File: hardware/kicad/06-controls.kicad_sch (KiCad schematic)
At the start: 38 parts, among them SW1 UP, SW10 SELECT, SW11 L, SW12 R, SW13 MENU, SW2 DOWN, SW3 LEFT, SW4 RIGHT, SW5 A, SW6 B, SW7 X, SW8 Y, SW9 START

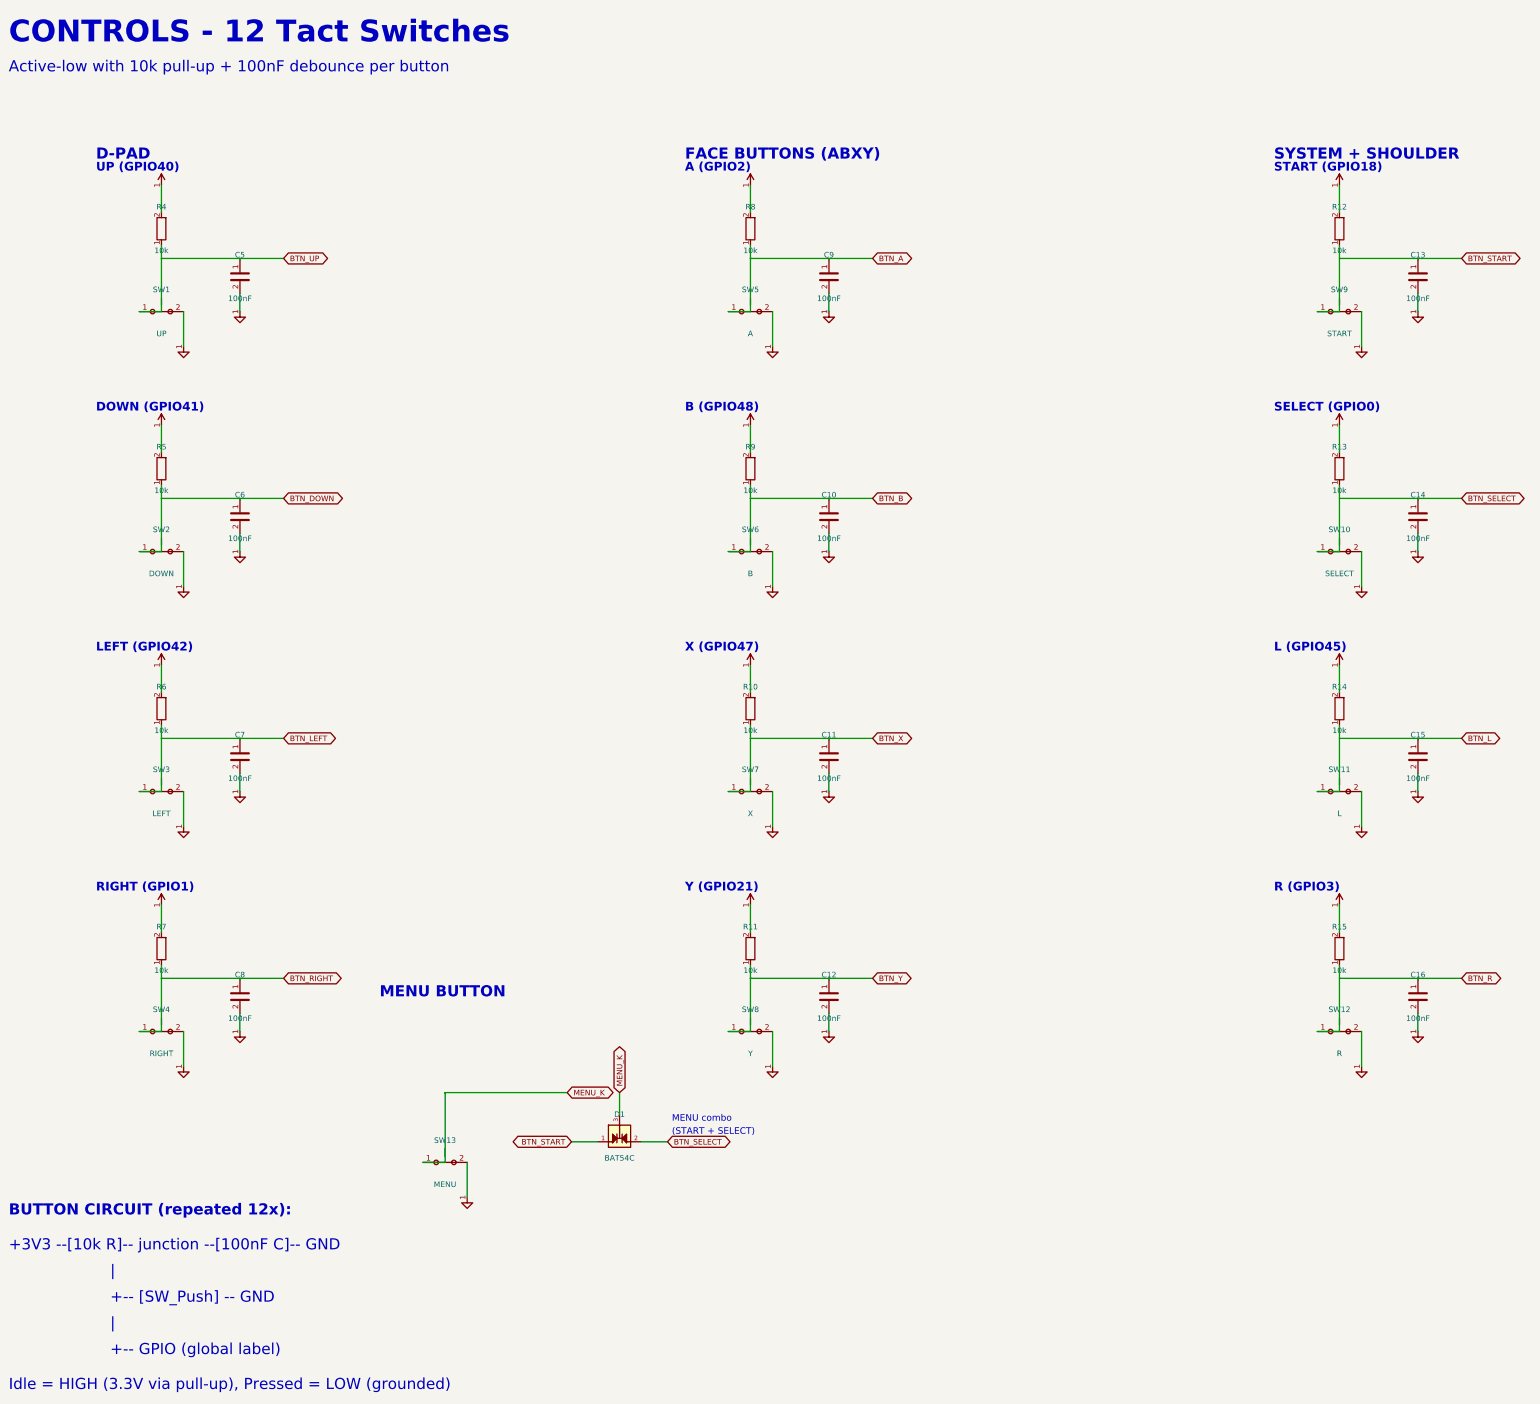
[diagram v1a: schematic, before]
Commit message: feat(containment): layer 6 — ERC warning burn-down, 676 to ZERO, gate at all severities
Three root causes, three fixes in the schematic generator:

- 507 endpoint_off_grid: sheets lay out on a human 1 mm grid while KiCad
  connects on 1.27 mm. snap() in kicad_primitives now grid-snaps every
  connection-bearing coordinate at emission. Snapping is monotonic and
  distributes over the library's grid-multiple pin offsets, so points
  that coincided before still coincide after; zero-length stub wires
  that collapse onto their anchor are dropped.
- The stragglers came from three symbols whose pin connection points
  were themselves off-grid: BAT54C (±5.0 → ±5.08, top 5.0 → 5.08, used
  by D1 and Q1), USBLC6-2SC6 (±10.0 → ±10.16), Speaker (±0.635 →
  ±1.27). Their sheet wiring moved with them in the same commit.
- 169 lib_symbol_issues: bare lib_ids referenced library "" which no
  configuration includes. Symbols are now emu:<name>, resolved by a
  generated hardware/kicad/sym-lib-table + emu.kicad_sym built from the
  same SYMBOLS strings as the embedded caches — cache and library
  cannot disagree by construction.

verify_erc now runs --severity-all against a ZERO baseline: from zero,
any new warning is a regression a specific change introduced. The
website's per-sheet SVGs/PDFs are re-rendered, and the "Download all
sheets" PDF — a one-off hand merge nothing regenerated, stale since the
R25 respin — is now merged by render-schematics.sh from the exported
sheets.

Suite: 85/85 green; netlist_diff vs PCB confirms connectivity unchanged.

Co-Authored-By: Claude Fable 5 <noreply@anthropic.com>
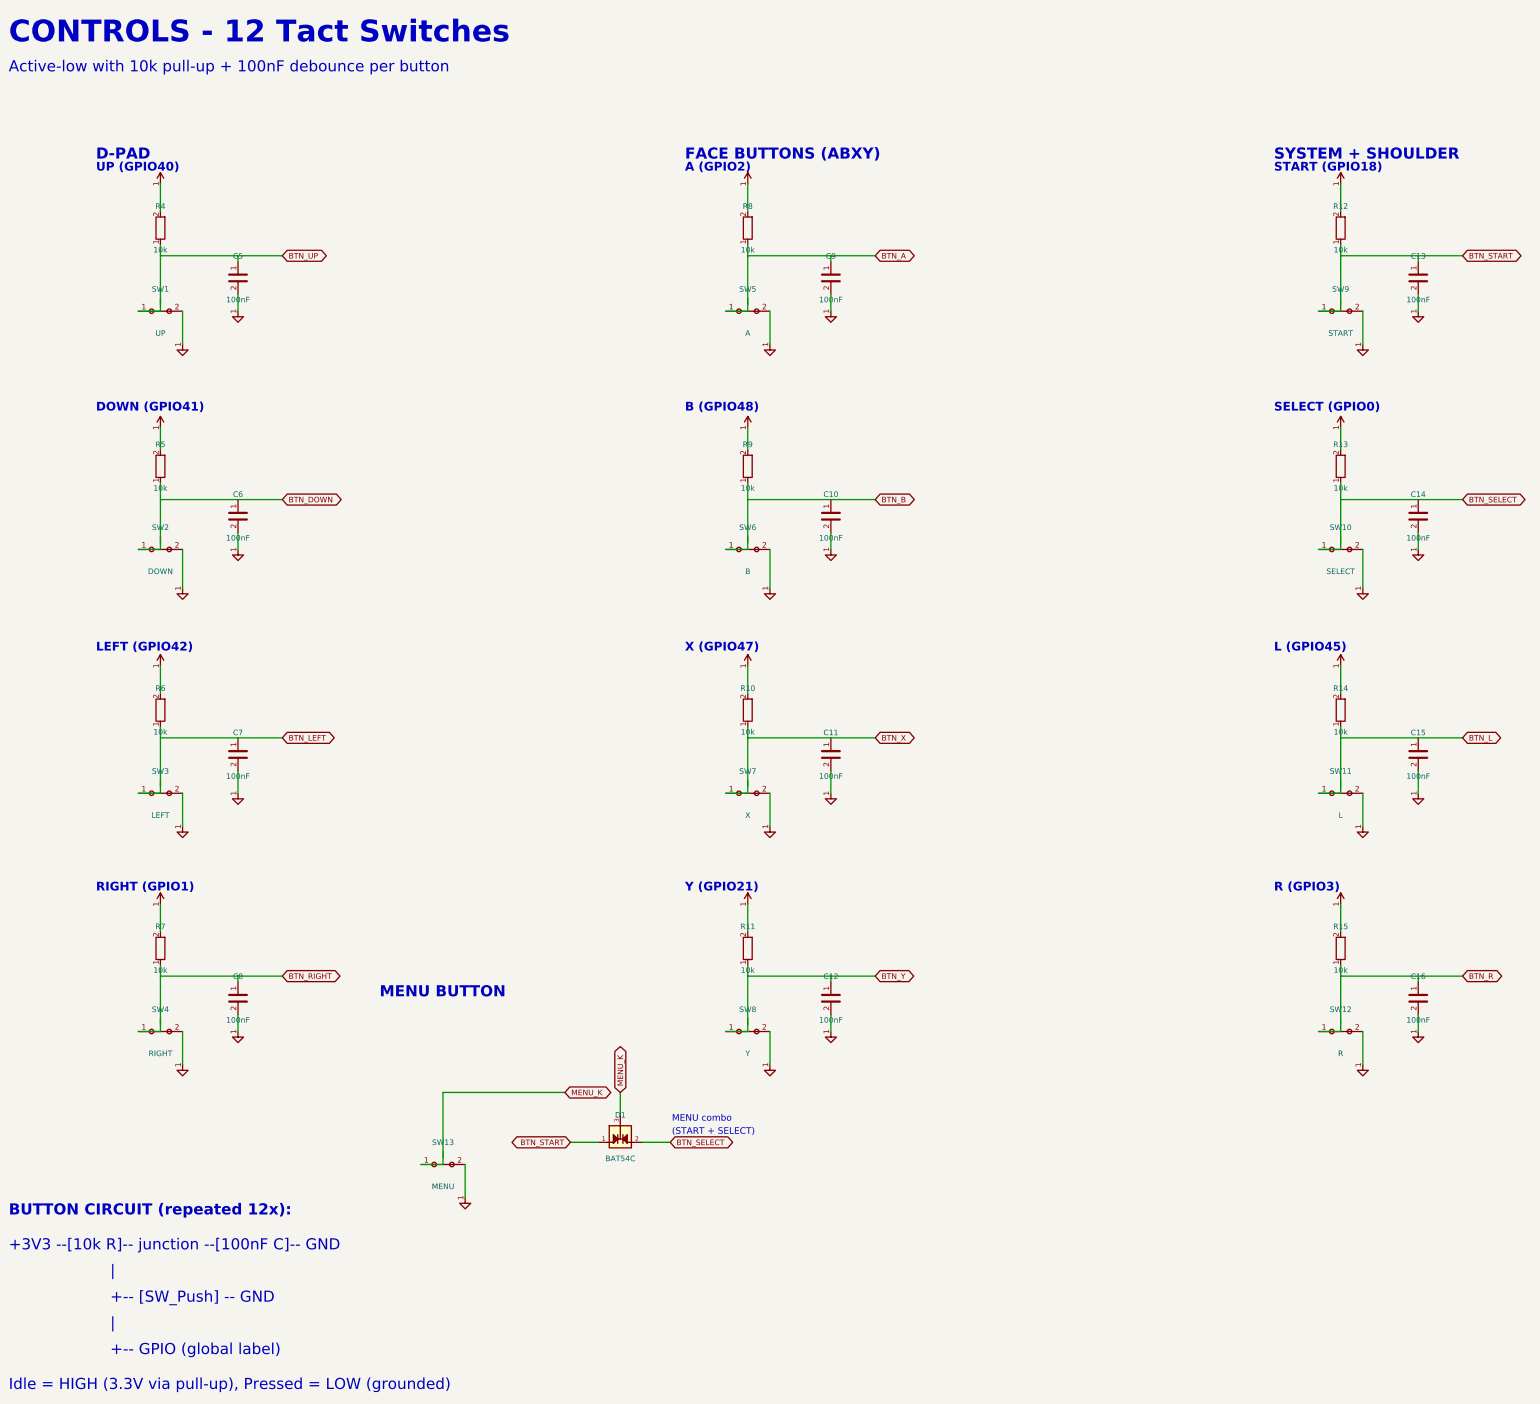
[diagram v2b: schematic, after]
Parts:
- removed C10, C11, C12, C13, C14, C15, C16, C7, C8, C9: 100nF, symbol C
- removed D1: BAT54C, symbol BAT54C
- removed R10, R11, R12, R13, R14, R6, R7, R8, R9: 10k, symbol R
- removed SW10: SELECT, symbol SW_Push
- removed SW11: L, symbol SW_Push
- removed SW12: R, symbol SW_Push
- removed SW13: MENU, symbol SW_Push
- removed SW2: DOWN, symbol SW_Push
- removed SW3: LEFT, symbol SW_Push
- removed SW4: RIGHT, symbol SW_Push
- removed SW5: A, symbol SW_Push
- removed SW6: B, symbol SW_Push
- removed SW7: X, symbol SW_Push
- removed SW8: Y, symbol SW_Push
- removed SW9: START, symbol SW_Push
- added C10, C11, C12, C13, C14, C15, C7, C8, C9: 100nF, symbol emu:C
- added D1: BAT54C, symbol emu:BAT54C
- added R10, R11, R12, R13, R14, R15, R6, R7, R8, R9: 10k, symbol emu:R
- added SW10: SELECT, symbol emu:SW_Push
- added SW11: L, symbol emu:SW_Push
- added SW12: R, symbol emu:SW_Push
- added SW13: MENU, symbol emu:SW_Push
- added SW2: DOWN, symbol emu:SW_Push
- added SW3: LEFT, symbol emu:SW_Push
- added SW4: RIGHT, symbol emu:SW_Push
- added SW5: A, symbol emu:SW_Push
- added SW6: B, symbol emu:SW_Push
- added SW7: X, symbol emu:SW_Push
- added SW8: Y, symbol emu:SW_Push
- added SW9: START, symbol emu:SW_Push
- C16: renamed from R15; value 10k -> 100nF; symbol R -> emu:C
- C5, C6: symbol C -> emu:C
- R4, R5: symbol R -> emu:R
- SW1: symbol SW_Push -> emu:SW_Push
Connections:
- net +3V3: now also R10.2, R11.2, R12.2, R13.2, R14.2, R15.2, R6.2, R7.2, R8.2, R9.2; no longer C16.2
- net BTN_A: now also C9.1, R8.1, SW5.1
- net BTN_B: now also C10.1, R9.1, SW6.1
- net BTN_DOWN: now also SW2.1
- net BTN_L: now also C15.1, R14.1, SW11.1
- net BTN_LEFT: now also C7.1, R6.1, SW3.1
- net BTN_R: now also R15.1, SW12.1
- net BTN_RIGHT: now also C8.1, R7.1, SW4.1
- net BTN_SELECT: now also C14.1, D1.2, R13.1, SW10.1
- net BTN_START: now also C13.1, D1.1, R12.1, SW9.1
- net BTN_X: now also C11.1, R10.1, SW7.1
- net BTN_Y: now also C12.1, R11.1, SW8.1
- net GND: now also C16.2, C10.2, C11.2, C12.2, C13.2, C14.2, C15.2, C7.2, C8.2, C9.2, SW10.2, SW11.2, SW12.2, SW13.2, SW2.2, SW3.2, SW4.2, SW5.2, SW6.2, SW7.2, SW8.2, SW9.2
- net MENU_K: now also D1.3, SW13.1
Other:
- moved on the sheet: C5, R5

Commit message: schematic: zero rendered text overlaps + real P-MOSFET artwork for Q1/Q2
The rendered sheets carried 75 text-on-text collisions the overlap gate
could not see: its model missed pin-number digits, KiCad's mirrored
field justification on 180-degree symbols, and global-label extents.
Root fixes in the generator:

- symbol() now places Reference/Value per part class: beside the body
  for two-pin verticals (R/C/L/Battery), stacked above for LEDs and the
  big ICs whose bottom pin numbers the old centred Value printed over,
  with per-call overrides where a zone is tight. On 180-rotated symbols
  the emitted justification is pre-mirrored, because KiCad flips it.
- Q1/Q2 get PMOS_SOT23 — same pin coordinates as the BAT54C symbol they
  were drawn with (wires and netlist untouched), but the artwork is now
  a P-MOSFET instead of a dual Schottky diode.
- Sheet-level relayouts: decoupling row on 02 spread to 11 mm pitch,
  menu-combo D1 zone on 06, FPC header on 03, PAM bias notes on 04,
  IP5306 KEY exit and the whole power-switch zone on 01.
- ESP32 module pin 41 name blanked — two "GND"s 2.54 mm apart printed
  into each other; number, type and net unchanged.

New gate: verify_schematic_render_overlaps.py exports each sheet to SVG
via kicad-cli and fails if any two DRAWN text runs intersect — ground
truth instead of a re-derived model (47 hits on the old sheet 01, 0
now). Wired into verify-all; dispatch mutation tests 14/14.

Netlist invariance: verify_netlist_diff 4/4, ERC clean at every
severity, schematic-PCB sync green. Website SVG/PDF re-rendered.

Co-Authored-By: Claude Fable 5 <noreply@anthropic.com>
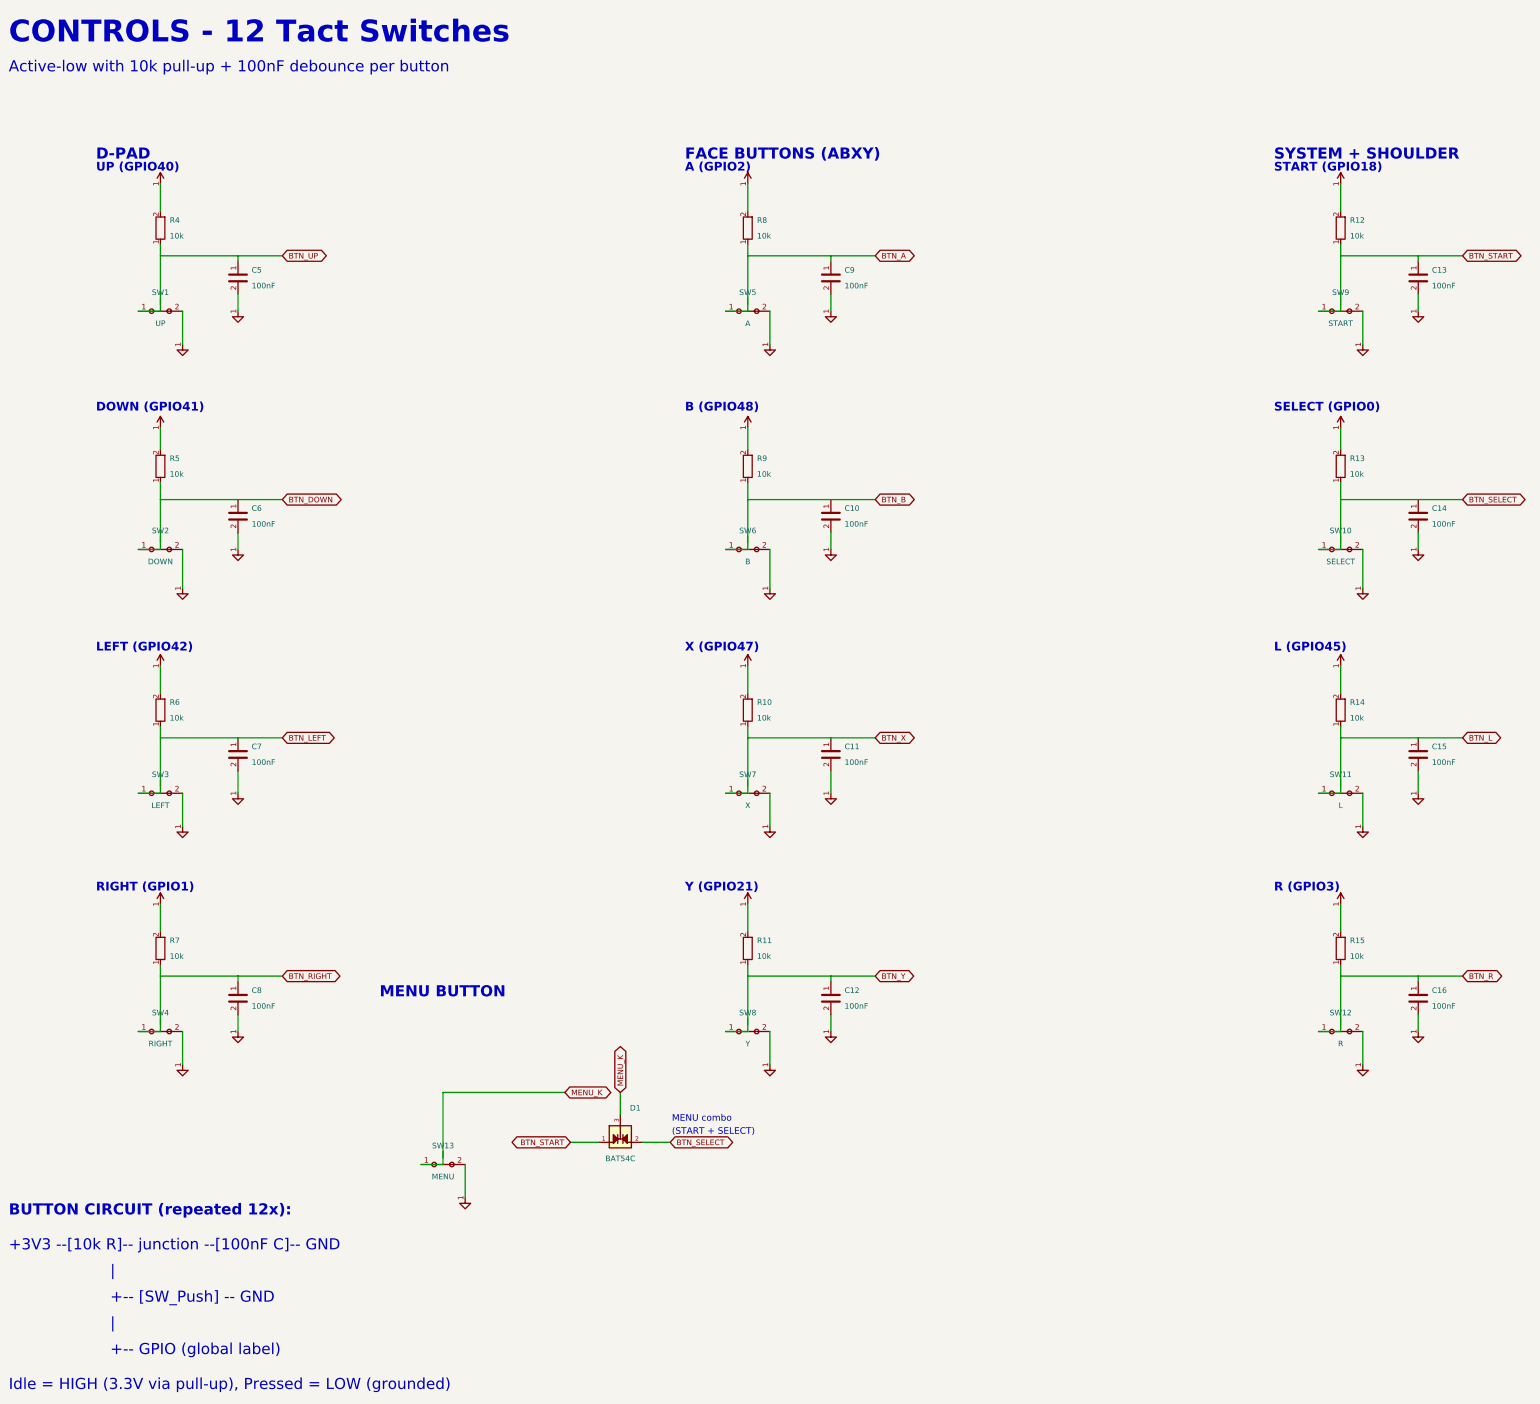
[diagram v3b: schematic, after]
